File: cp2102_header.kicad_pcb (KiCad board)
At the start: 2 copper layers, 15.2 x 22.9 mm, 32 parts, among them J1 FTDI, J2 USB_B_Micro, J22 USB_B_Micro, J8 mount, Q3 BSS138PS, Q4 BSS138PS, U2 CP2102N

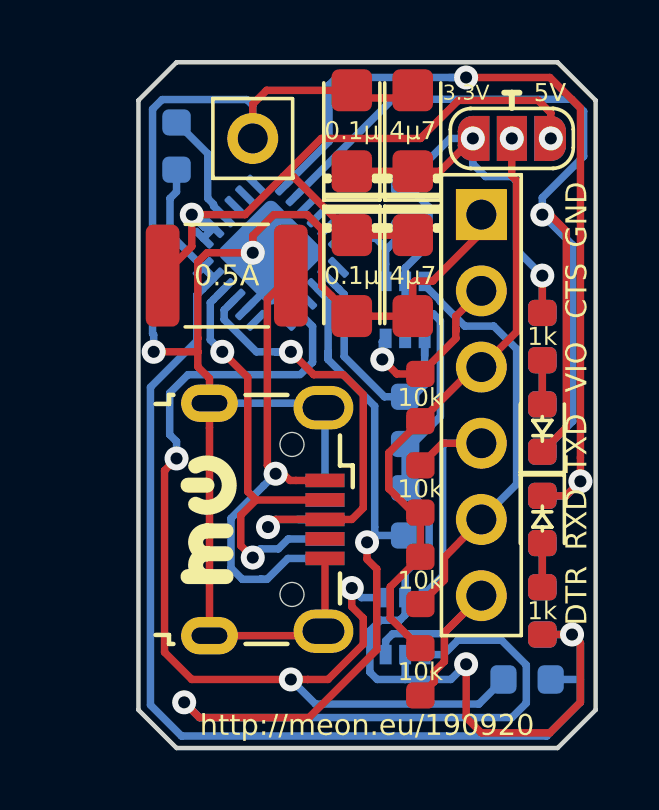
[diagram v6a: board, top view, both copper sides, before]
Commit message: switch to 0.5A trip current fuse
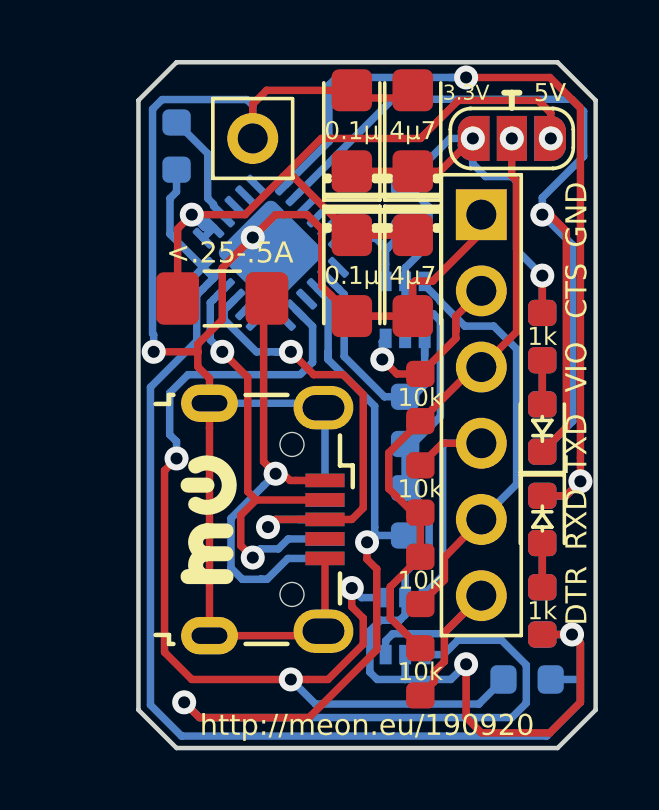
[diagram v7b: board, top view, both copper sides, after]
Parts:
- F2: footprint Fuse:Fuse_1812_4532Metric -> Fuse:Fuse_1206_3216Metric_Pad1.42x1.75mm_HandSolder
- moved F2 0.78 mm to (80.3, 79.0)
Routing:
- net GND: track 64.6 -> 63.7 mm
- net Net-(F2-Pad2): track 16.2 -> 15.6 mm
- net +5V: track 24.7 -> 25.3 mm
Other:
- board text added: "<.25-.5A"
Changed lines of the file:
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@@
   (general
     (thickness 1.6)
-    (drawings 47)
-    (tracks 362)
+    (drawings 48)
+    (tracks 363)
     (zones 0)
     (modules 32)
@@
       (net 2 GND))
     (model ${KISYS3DMOD}/Capacitor_Tantalum_SMD.3dshapes/CP_EIA-3216-18_Kemet-A.wrl
-      (at (xyz 0 0 0))
-      (scale (xyz 1 1 1))
-      (rotate (xyz 0 0 0))
-    )
-  )
-  (module Fuse:Fuse_1812_4532Metric (layer F.Cu)
-    (at 80.4125 78.232)
-    (descr "Fuse SMD 1812 (4532 Metric), square (rectangular) end terminal, IPC_7351 nominal, (Body size source: https://www.nikhef.nl/pub/departments/mt/projects/detectorR_D/dtddice/ERJ2G.pdf), generated with kicad-footprint-generator")
-    (tags resistor)
-    (attr smd)
-    (fp_text reference F2 (at 0 -2.65) (layer F.SilkS) hide
-      (effects (font (size 1 1) (thickness 0.15)))
-    )
-    (fp_text value 0.5A (at 0 0) (layer F.SilkS)
-      (effects (font (size 0.7 0.7) (thickness 0.125)))
-    )
-    (fp_line (start -2.25 1.6) (end -2.25 -1.6) (layer F.Fab) (width 0.1))
-    (fp_line (start -2.25 -1.6) (end 2.25 -1.6) (layer F.Fab) (width 0.1))
-    (fp_line (start 2.25 -1.6) (end 2.25 1.6) (layer F.Fab) (width 0.1))
-    (fp_line (start 2.25 1.6) (end -2.25 1.6) (layer F.Fab) (width 0.1))
-    (fp_line (start -1.386252 -1.71) (end 1.386252 -1.71) (layer F.SilkS) (width 0.12))
-    (fp_line (start -1.386252 1.71) (end 1.386252 1.71) (layer F.SilkS) (width 0.12))
-    (fp_line (start -2.95 1.95) (end -2.95 -1.95) (layer F.CrtYd) (width 0.05))
-    (fp_line (start -2.95 -1.95) (end 2.95 -1.95) (layer F.CrtYd) (width 0.05))
-    (fp_line (start 2.95 -1.95) (end 2.95 1.95) (layer F.CrtYd) (width 0.05))
-    (fp_line (start 2.95 1.95) (end -2.95 1.95) (layer F.CrtYd) (width 0.05))
-    (fp_text user %R (at 0 0) (layer F.Fab) hide
-      (effects (font (size 1 1) (thickness 0.15)))
-    )
-    (pad 1 smd roundrect (at -2.1375 0) (size 1.125 3.4) (layers F.Cu F.Paste F.Mask) (roundrect_rratio 0.222222)
-      (net 3 +5V))
-    (pad 2 smd roundrect (at 2.1375 0) (size 1.125 3.4) (layers F.Cu F.Paste F.Mask) (roundrect_rratio 0.222222)
-      (net 20 "Net-(F2-Pad2)"))
-    (model ${KISYS3DMOD}/Fuse.3dshapes/Fuse_1812_4532Metric.wrl
       (at (xyz 0 0 0))
       (scale (xyz 1 1 1))
@@
       (rotate (xyz 0 0 0))
     )
+  )
+  (module Fuse:Fuse_1206_3216Metric_Pad1.42x1.75mm_HandSolder (layer F.Cu)
+    (at 80.264 78.994)
+    (descr "Fuse SMD 1206 (3216 Metric), square (rectangular) end terminal, IPC_7351 nominal with elongated pad for handsoldering. (Body size source: http://www.tortai-tech.com/upload/download/2011102023233369053.pdf), generated with kicad-footprint-generator")
+    (tags "resistor handsolder")
+    (attr smd)
+    (fp_text reference F2 (at 0 -1.82) (layer F.SilkS) hide
+      (effects (font (size 1 1) (thickness 0.15)))
+    )
+    (fp_text value 0.5A (at 0 1.82) (layer F.Fab)
+      (effects (font (size 1 1) (thickness 0.15)))
+    )
+    (fp_line (start -1.6 0.8) (end -1.6 -0.8) (layer F.Fab) (width 0.1))
+    (fp_line (start -1.6 -0.8) (end 1.6 -0.8) (layer F.Fab) (width 0.1))
+    (fp_line (start 1.6 -0.8) (end 1.6 0.8) (layer F.Fab) (width 0.1))
+    (fp_line (start 1.6 0.8) (end -1.6 0.8) (layer F.Fab) (width 0.1))
+    (fp_line (start -0.602064 -0.91) (end 0.602064 -0.91) (layer F.SilkS) (width 0.12))
+    (fp_line (start -0.602064 0.91) (end 0.602064 0.91) (layer F.SilkS) (width 0.12))
+    (fp_line (start -2.45 1.12) (end -2.45 -1.12) (layer F.CrtYd) (width 0.05))
+    (fp_line (start -2.45 -1.12) (end 2.45 -1.12) (layer F.CrtYd) (width 0.05))
+    (fp_line (start 2.45 -1.12) (end 2.45 1.12) (layer F.CrtYd) (width 0.05))
+    (fp_line (start 2.45 1.12) (end -2.45 1.12) (layer F.CrtYd) (width 0.05))
+    (fp_text user %R (at 0 0) (layer F.Fab)
+      (effects (font (size 0.8 0.8) (thickness 0.12)))
+    )
+    (pad 1 smd roundrect (at -1.4875 0) (size 1.425 1.75) (layers F.Cu F.Paste F.Mask) (roundrect_rratio 0.175439)
+      (net 3 +5V))
+    (pad 2 smd roundrect (at 1.4875 0) (size 1.425 1.75) (layers F.Cu F.Paste F.Mask) (roundrect_rratio 0.175439)
+      (net 20 "Net-(F2-Pad2)"))
+    (model ${KISYS3DMOD}/Fuse.3dshapes/Fuse_1206_3216Metric.wrl
+      (at (xyz 0 0 0))
+      (scale (xyz 1 1 1))
+      (rotate (xyz 0 0 0))
+    )
+  )
+  (gr_text <.25-.5A (at 80.518 77.47) (layer F.SilkS)
+    (effects (font (size 0.7 0.7) (thickness 0.15)))
   )
   (gr_line (start 83.693 74.93) (end 83.82 74.93) (layer F.SilkS) (width 0.2))
@@
   (segment (start 81.042811 79.370349) (end 81.8825 78.53066) (width 0.25) (layer B.Cu) (net 2))
   (segment (start 83.688 90.035) (end 83.638 90.085) (width 0.25) (layer F.Cu) (net 2) (status 30))
-  (via (at 81.28 77.47) (size 0.8) (drill 0.4) (layers F.Cu B.Cu) (net 2))
+  (via (at 81.28 76.962) (size 0.8) (drill 0.4) (layers F.Cu B.Cu) (net 2))
   (segment (start 83.488 82.485) (end 83.638 82.635) (width 0.25) (layer B.Cu) (net 2) (status 30))
   (segment (start 79.838 82.485) (end 79.838 81.66) (width 0.25) (layer F.Cu) (net 2) (status 10))
@@
   (segment (start 79.838 82.485) (end 83.488 82.485) (width 0.25) (layer B.Cu) (net 2) (status 30))
   (segment (start 79.45 81.272) (end 79.45 80.772) (width 0.25) (layer F.Cu) (net 2))
-  (segment (start 79.45 80.772) (end 79.45 80.316) (width 0.25) (layer F.Cu) (net 2))
   (segment (start 79.838 90.235) (end 83.488 90.235) (width 0.25) (layer F.Cu) (net 2) (status 30))
   (segment (start 83.688 87.66) (end 83.688 90.035) (width 0.25) (layer F.Cu) (net 2) (status 30))
@@
   (via (at 77.978 80.772) (size 0.8) (drill 0.4) (layers F.Cu B.Cu) (net 2))
   (segment (start 79.45 80.772) (end 77.978 80.772) (width 0.25) (layer F.Cu) (net 2))
-  (segment (start 79.45 80.316) (end 79.45 77.776) (width 0.25) (layer F.Cu) (net 2))
-  (segment (start 79.756 77.47) (end 81.28 77.47) (width 0.25) (layer F.Cu) (net 2))
-  (segment (start 79.45 77.776) (end 79.756 77.47) (width 0.25) (layer F.Cu) (net 2))
-  (segment (start 81.28 77.47) (end 81.28 76.904315) (width 0.25) (layer F.Cu) (net 2))
   (segment (start 87.27718 78.41501) (end 86.68499 78.41501) (width 0.25) (layer F.Cu) (net 2))
   (segment (start 86.614 78.486) (end 86.614 79.582) (width 0.25) (layer F.Cu) (net 2))
@@
   (segment (start 83.58199 76.6883) (end 83.58199 78.58199) (width 0.25) (layer F.Cu) (net 2))
   (segment (start 83.09369 76.2) (end 83.58199 76.6883) (width 0.25) (layer F.Cu) (net 2))
-  (segment (start 81.984315 76.2) (end 83.09369 76.2) (width 0.25) (layer F.Cu) (net 2))
   (segment (start 83.58199 78.58199) (end 83.897627 78.897627) (width 0.25) (layer F.Cu) (net 2))
-  (segment (start 81.28 76.904315) (end 81.984315 76.2) (width 0.25) (layer F.Cu) (net 2))
   (segment (start 77.93999 72.68201) (end 78.25801 72.36399) (width 0.25) (layer B.Cu) (net 2))
   (segment (start 77.978 80.206315) (end 77.93999 80.168305) (width 0.25) (layer B.Cu) (net 2))
@@
   (segment (start 81.741 72.056) (end 81.28 72.517) (width 0.25) (layer F.Cu) (net 2))
   (segment (start 81.28 72.517) (end 81.28 73.66) (width 0.25) (layer F.Cu) (net 2))
+  (segment (start 80.264 77.978) (end 81.28 76.962) (width 0.25) (layer F.Cu) (net 2))
+  (segment (start 80.264 79.698998) (end 80.264 77.978) (width 0.25) (layer F.Cu) (net 2))
+  (segment (start 79.45 80.772) (end 79.45 80.512998) (width 0.25) (layer F.Cu) (net 2))
+  (segment (start 79.45 80.512998) (end 80.264 79.698998) (width 0.25) (layer F.Cu) (net 2))
+  (segment (start 82.042 76.2) (end 82.296 76.2) (width 0.25) (layer F.Cu) (net 2))
+  (segment (start 81.28 76.962) (end 82.042 76.2) (width 0.25) (layer F.Cu) (net 2))
+  (segment (start 82.296 76.2) (end 83.09369 76.2) (width 0.25) (layer F.Cu) (net 2))
   (segment (start 79.628598 76.983864) (end 79.982151 76.630311) (width 0.25) (layer B.Cu) (net 3))
   (segment (start 79.628597 76.983864) (end 79.628598 76.983864) (width 0.25) (layer B.Cu) (net 3))
@@
   (via (at 79.248 76.2) (size 0.8) (drill 0.4) (layers F.Cu B.Cu) (net 3))
   (via (at 91.216 73.66) (size 0.8) (drill 0.4) (layers F.Cu B.Cu) (net 3))
-  (segment (start 79.248 77.259) (end 78.275 78.232) (width 0.25) (layer F.Cu) (net 3))
-  (segment (start 79.248 76.2) (end 79.248 77.259) (width 0.25) (layer F.Cu) (net 3))
   (segment (start 91.216 72.812408) (end 91.216 73.66) (width 0.25) (layer F.Cu) (net 3))
   (segment (start 79.248 76.2) (end 81.025002 76.2) (width 0.25) (layer F.Cu) (net 3))
@@
   (segment (start 82.629002 74.929002) (end 82.296 74.929002) (width 0.25) (layer F.Cu) (net 3))
   (segment (start 82.296 74.929002) (end 83.565002 73.66) (width 0.25) (layer F.Cu) (net 3))
+  (segment (start 78.7765 76.6715) (end 79.248 76.2) (width 0.25) (layer F.Cu) (net 3))
+  (segment (start 78.7765 78.994) (end 78.7765 76.6715) (width 0.25) (layer F.Cu) (net 3))
   (segment (start 90.932 82.5245) (end 90.932 81.0515) (width 0.25) (layer F.Cu) (net 4) (status 30))
   (segment (start 90.932 88.6205) (end 90.932 87.1475) (width 0.25) (layer F.Cu) (net 5) (status 30))
@@
   (segment (start 81.534 88.355001) (end 80.931999 88.355001) (width 0.25) (layer B.Cu) (net 20))
   (segment (start 82.042 84.836) (end 81.767592 84.561592) (width 0.25) (layer F.Cu) (net 20))
-  (segment (start 81.767592 79.014408) (end 82.55 78.232) (width 0.25) (layer F.Cu) (net 20))
-  (segment (start 81.767592 84.561592) (end 81.767592 79.014408) (width 0.25) (layer F.Cu) (net 20))
+  (segment (start 81.642001 79.103499) (end 81.7515 78.994) (width 0.25) (layer F.Cu) (net 20))
+  (segment (start 81.642001 84.436001) (end 81.642001 79.103499) (width 0.25) (layer F.Cu) (net 20))
+  (segment (start 82.042 84.836) (end 81.642001 84.436001) (width 0.25) (layer F.Cu) (net 20))
   (segment (start 90.932 82.5245) (end 90.932 81.0515) (width 0.25) (layer B.Cu) (net 21))
   (segment (start 90.932 87.1475) (end 90.932 88.6205) (width 0.25) (layer B.Cu) (net 22))

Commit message: move extra gnd pin
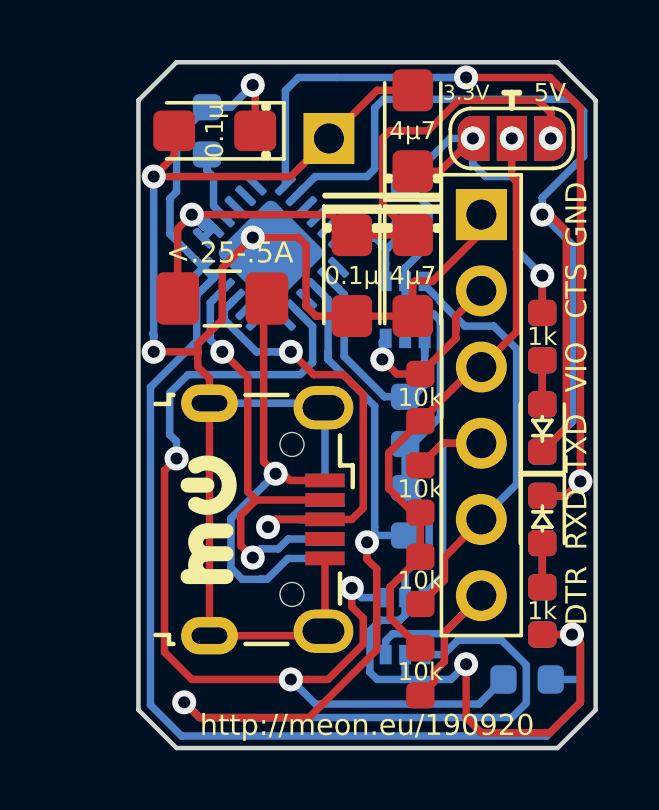
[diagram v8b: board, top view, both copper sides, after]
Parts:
- J8: footprint Connector_PinHeader_2.54mm:PinHeader_1x01_P2.54mm_Vertical_closed -> Connector_PinHeader_2.54mm:PinHeader_1x01_P2.54mm_Vertical_no_lines
- moved C22 4.57 mm to (80.0, 73.4), turned to 180 degrees
- moved J8 2.54 mm to (83.8, 73.7)
- moved R2 1.14 mm to (79.8, 73.4), turned to 90 degrees
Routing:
- net +3V3: track 90.1 -> 93.7 mm, vias 4 -> 5
- net GND: track 63.7 -> 60.7 mm, vias 2 -> 3
- net Net-(R2-Pad1): track 3.81 -> 2.32 mm
- net +5V: track 25.3 -> 24.0 mm
- net TXL: track 32.3 -> 33.5 mm
- net RXL: track 28.5 -> 29.3 mm
